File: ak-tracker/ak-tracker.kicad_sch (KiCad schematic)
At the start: 0 parts

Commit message: docs
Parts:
- added U1: (no value), symbol 1_JP:BMA400
- added U2: TPL5010, Package_TO_SOT_SMD:SOT-23-6, symbol Timer:TPL5010
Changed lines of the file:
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@@
 (kicad_sch
-	(version 20250114)
+	(version 20260306)
 	(generator "eeschema")
-	(generator_version "9.0")
+	(generator_version "10.0")
 	(paper "A4")
+	(symbol
+		(lib_id "Timer:TPL5010")
+		(at 73.66 101.6 0)
+		(unit 1)
+		(body_style 1)
+		(exclude_from_sim no)
+		(in_bom yes)
+		(on_board yes)
+		(in_pos_files yes)
+		(dnp no)
+		(fields_autoplaced yes)
+		(property "Reference" "U2"
+			(at 75.8033 88.9 0)
+			(show_name no)
+			(do_not_autoplace no)
+			(effects
+				(font
+					(size 1.27 1.27)
+				)
+				(justify left)
+			)
+		)
+		(property "Value" "TPL5010"
+			(at 75.8033 91.44 0)
+			(show_name no)
+			(do_not_autoplace no)
+			(effects
+				(font
+					(size 1.27 1.27)
+				)
+				(justify left)
+			)
+		)
+		(property "Footprint" "Package_TO_SOT_SMD:SOT-23-6"
+			(at 73.66 101.6 0)
+			(hide yes)
+			(show_name no)
+			(do_not_autoplace no)
+			(effects
+				(font
+					(size 1.27 1.27)
+				)
+			)
+		)
+		(property "Datasheet" "http://www.ti.com/lit/ds/symlink/tpl5010.pdf"
+			(at 68.58 109.22 0)
+			(hide yes)
+			(show_name no)
+			(do_not_autoplace no)
+			(effects
+				(font
+					(size 1.27 1.27)
+				)
+			)
+		)
+		(property "Description" "Timer, Nano Power, Watchdog, 35 nA, 100 ms to 7200 s, VDD 1.8V to 5.5V, Iout max 1mA"
+			(at 73.66 101.6 0)
+			(hide yes)
+			(show_name no)
+			(do_not_autoplace no)
+			(effects
+				(font
+					(size 1.27 1.27)
+				)
+			)
+		)
+		(pin "1"
+		)
+		(pin "2"
+		)
+		(pin "3"
+		)
+		(pin "4"
+		)
+		(pin "5"
+		)
+		(pin "6"
+		)
+		(instances
+			(project "ak-tracker"
+				(path "/c9a4dcbd-d029-4d79-afa4-833091072a3d"
+					(reference "U2")
+					(unit 1)
+				)
+			)
+		)
+	)
+	(symbol
+		(lib_id "1_JP:BMA400")
+		(at 63.5 55.88 0)
+		(unit 1)
+		(body_style 1)
+		(exclude_from_sim no)
+		(in_bom yes)
+		(on_board yes)
+		(in_pos_files yes)
+		(dnp no)
+		(property "Reference" "U1"
+			(at 79.502 49.53 0)
+			(show_name no)
+			(do_not_autoplace no)
+			(effects
+				(font
+					(size 1.27 1.27)
+				)
+			)
+		)
+		(property "Value" ""
+			(at 63.5 55.88 0)
+			(show_name no)
+			(do_not_autoplace no)
+			(effects
+				(font
+					(size 1.27 1.27)
+				)
+			)
+		)
+		(property "Footprint" ""
+			(at 63.5 55.88 0)
+			(hide yes)
+			(show_name no)
+			(do_not_autoplace no)
+			(effects
+				(font
+					(size 1.27 1.27)
+				)
+			)
+		)
+		(property "Datasheet" ""
+			(at 63.5 55.88 0)
+			(hide yes)
+			(show_name no)
+			(do_not_autoplace no)
+			(effects
+				(font
+					(size 1.27 1.27)
+				)
+			)
+		)
+		(property "Description" ""
+			(at 63.5 55.88 0)
+			(hide yes)
+			(show_name no)
+			(do_not_autoplace no)
+			(effects
+				(font
+					(size 1.27 1.27)
+				)
+			)
+		)
+		(pin "8"
+		)
+		(pin "10"
+		)
+		(pin "9"
+		)
+		(pin "6"
+		)
+		(pin "7"
+		)
+		(pin "12"
+		)
+		(pin "4"
+		)
+		(pin "11"
+		)
+		(pin "2"
+		)
+		(pin "3"
+		)
+		(pin "1"
+		)
+		(pin "5"
+		)
+		(instances
+			(project "ak-tracker"
+				(path "/c9a4dcbd-d029-4d79-afa4-833091072a3d"
+					(reference "U1")
+					(unit 1)
+				)
+			)
+		)
+	)
 	(sheet_instances
 		(path "/"

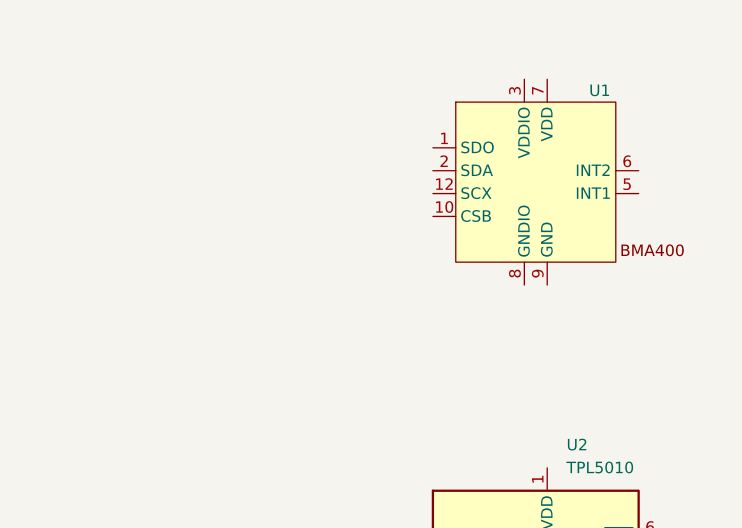
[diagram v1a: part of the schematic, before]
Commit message: TPL5010 and BMA400 as symbols in KiCad
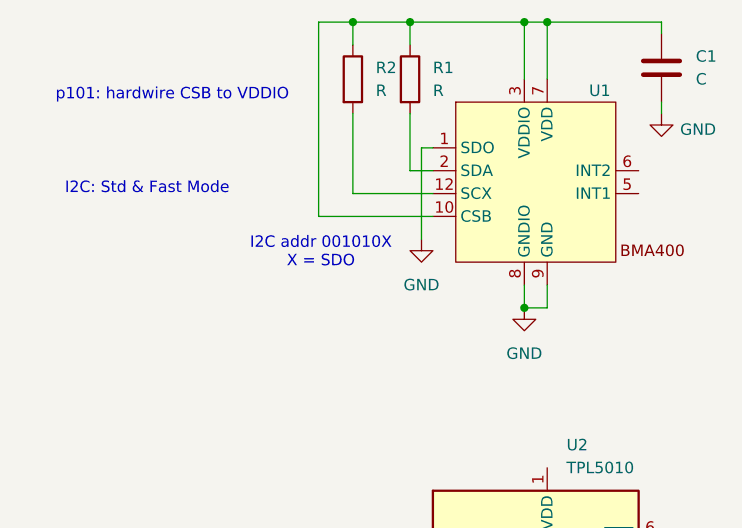
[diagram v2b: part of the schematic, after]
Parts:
- added C1: C, symbol Device:C
- added R1, R2: R, symbol Device:R
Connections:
- net GND: now reaches U1.1 (SDO)
- net GND: now also U1.8 (GNDIO), U1.9 (GND), C1.2
- net at U1.10 (CSB): now also U1.3 (VDDIO), U1.7 (VDD), C1.1, R1.1, R2.1
- net at U1.12 (SCX): now also R2.2
- net at U1.2 (SDA): now also R1.2
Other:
- note added: "I2C addr 001010X X = SDO"
- note added: "I2C: Std & Fast Mode"
- note added: "p101: hardwire CSB to VDDIO"

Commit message: initial schematic
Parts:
- added C2: C, symbol Device:C
- added J1: left, Connector_PinHeader_2.54mm:PinHeader_1x18_P2.54mm_Vertical, symbol Connector_Generic:Conn_01x18
- added J2: right, Connector_PinHeader_2.54mm:PinHeader_1x18_P2.54mm_Vertical, symbol Connector_Generic:Conn_01x18
- added R3, R4: 47k, symbol Device:R
- added SW1: Reset, symbol Switch:SW_Push
- added SW2: SW_DIP_x01, symbol Switch:SW_DIP_x01
- U1: value (none) -> BMA400
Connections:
- net GND: now also U2.2 (GND), C2.2, J1.2 (Pin_2), J2.2 (Pin_2), R4.2
- net at U2.1 (VDD): now also C2.1, R3.1, SW1.2, SW2.1
- net at U2.3 (DELAY/M_RST): now also R4.1, SW1.1
- net WOKE: now reaches U2.4 (DONE)
- net WAKE: now reaches U2.5 (WAKE)
- net ~{RST}: now reaches U2.6 (~{RST})
- net ~{RST}: now also J2.18 (Pin_18), R3.2
- net VCC: now reaches C1.1, R1.1, R2.1, U1.10 (CSB), U1.3 (VDDIO), U1.7 (VDD)
- net VCC: now also J2.3 (Pin_3), SW2.2
- net SCL: now reaches R2.2, U1.12 (SCX)
- net SCL: now also J1.6 (Pin_6)
- net SDA: now reaches R1.2, U1.2 (SDA)
- net SDA: now also J1.7 (Pin_7)
- new net VEXT: J1.3 (Pin_3)
- no-connect marks 0 -> 4
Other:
- note added: "2 x 18 x 2.54 mm 25.4? mm apart"
- note added: "~6min"
- moved on the sheet: R1, R2

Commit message: footprints
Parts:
- removed SW2: SW_DIP_x01, symbol Switch:SW_DIP_x01
- added SW3: SW_DIP_x02, Button_Switch_SMD:SW_DIP_SPSTx02_Slide_6.7x6.64mm_W6.73mm_P2.54mm_LowProfile_JPin, symbol Switch:SW_DIP_x02
- C1, C2: footprint (none) -> Capacitor_SMD:C_0805_2012Metric_Pad1.18x1.45mm_HandSolder
- R1, R2: value R -> 2k2; footprint (none) -> Resistor_SMD:R_0805_2012Metric_Pad1.20x1.40mm_HandSolder
- R3: value 47k -> 100k; footprint (none) -> Resistor_SMD:R_0805_2012Metric_Pad1.20x1.40mm_HandSolder
- R4: footprint (none) -> Resistor_SMD:R_0805_2012Metric_Pad1.20x1.40mm_HandSolder
- SW1: footprint (none) -> Button_Switch_SMD:SW_Push_1P1T_NO_CK_KSC9xxG
- U1: footprint (none) -> Package_LGA:LGA-12_2x2mm_P0.5mm
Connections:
- net VCC: now also SW3.3, SW3.4; no longer C1.1, R1.1, R2.1, U1.10 (CSB), U1.3 (VDDIO), U1.7 (VDD)
- net WAKE: now also J2.8 (Pin_8)
- net WOKE: now also J2.7 (Pin_7)
- net at C2.1, R3.1, SW1.2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: now also SW3.2
- net MOVED: now reaches J2.6 (Pin_6)
- net MOVED: now also U1.5 (INT1)
- new net: C1.1, R1.1, R2.1, SW3.1, U1.10 (CSB), U1.3 (VDDIO), U1.7 (VDD)
- no-connect marks 4 -> 27
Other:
- note added: "For BMI270, use BMI160 symbol"
- note added: "No intr really needed for atonomous mode"

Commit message: initial routing
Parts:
- removed SW1: Reset, Button_Switch_SMD:SW_Push_1P1T_NO_CK_KSC9xxG, symbol Switch:SW_Push
- added R5: 0, Resistor_SMD:R_0805_2012Metric_Pad1.20x1.40mm_HandSolder, symbol Device:R
- added SW2: Reset, Button_Switch_SMD:SW_Push_1P1T_NO_CK_KSC9xxG, symbol Switch:SW_Push
- SW3: footprint Button_Switch_SMD:SW_DIP_SPSTx02_Slide_6.7x6.64mm_W6.73mm_P2.54mm_LowProfile_JPin -> Button_Switch_SMD:SW_DIP_SPSTx02_Slide_9.78x7.26mm_W8.61mm_P2.54mm
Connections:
- net VDD2: now reaches C2.1, R3.1, U2.1 (VDD)
- net VDD2: now also SW3.1, SW2.2; no longer SW3.2
- net at R4.1, U2.3 (DELAY/M_RST): now also SW2.1
- net VDD1: now reaches C1.1, R2.1, U1.10 (CSB), U1.7 (VDD)
- net VDD1: now also SW3.2, R5.2; no longer R1.1, SW3.1, U1.3 (VDDIO)
- new net: R1.1, R5.1, U1.3 (VDDIO)

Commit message: better routing
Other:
- moved on the sheet: R1, R2, R5

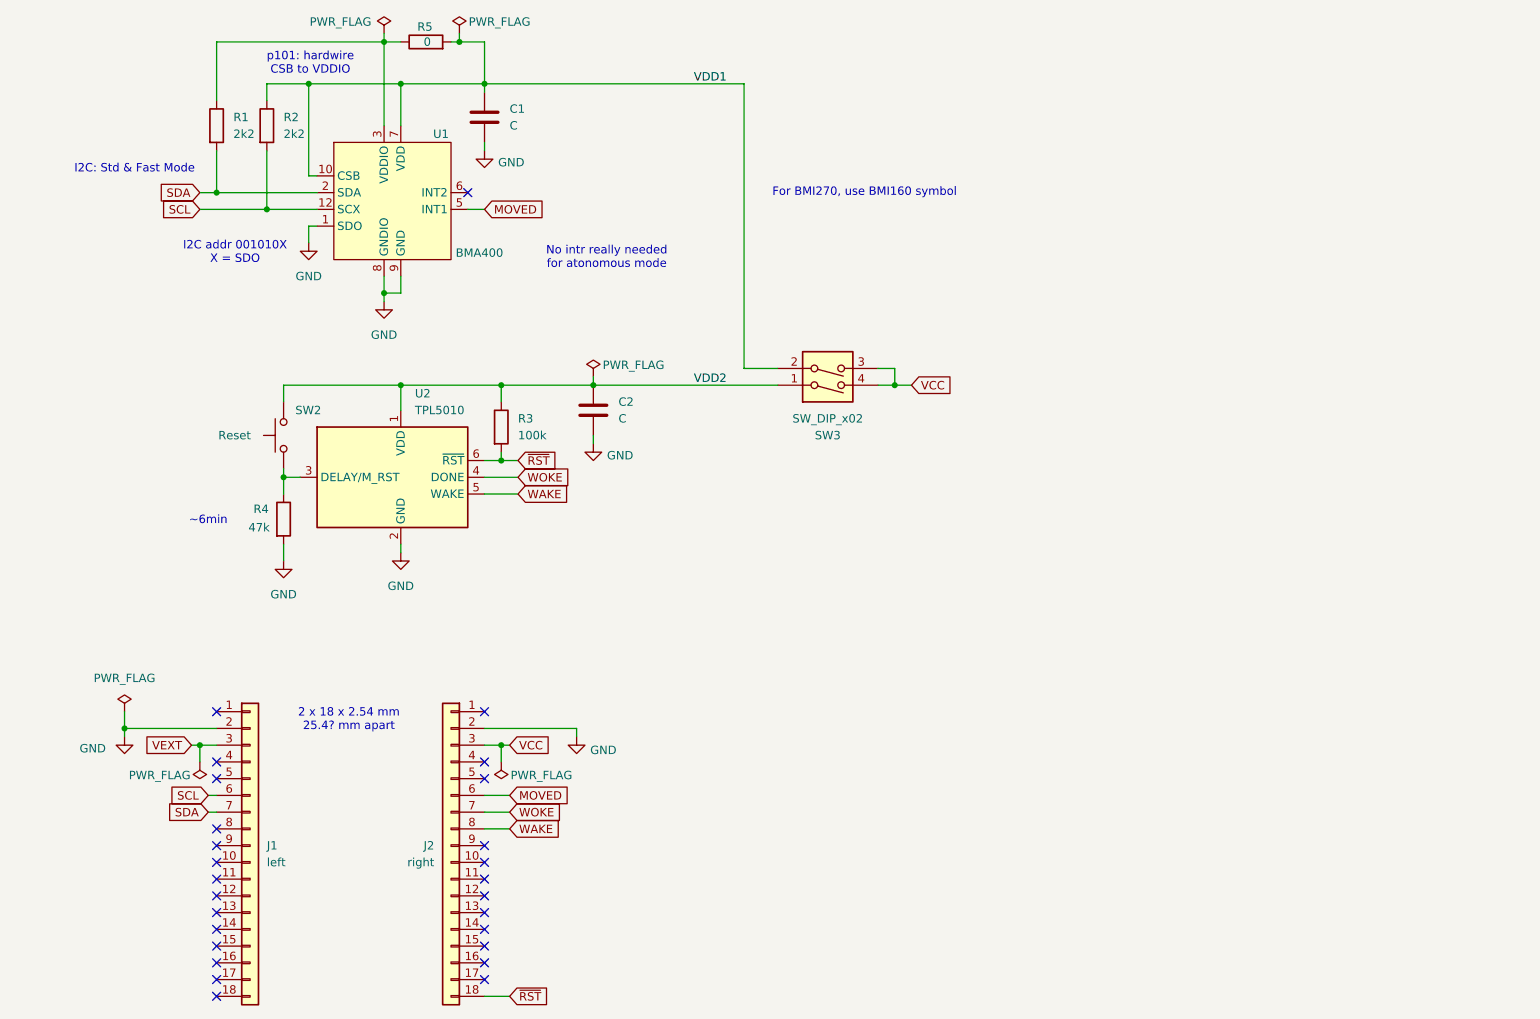
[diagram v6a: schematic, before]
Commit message: interrupts to 5,6,7
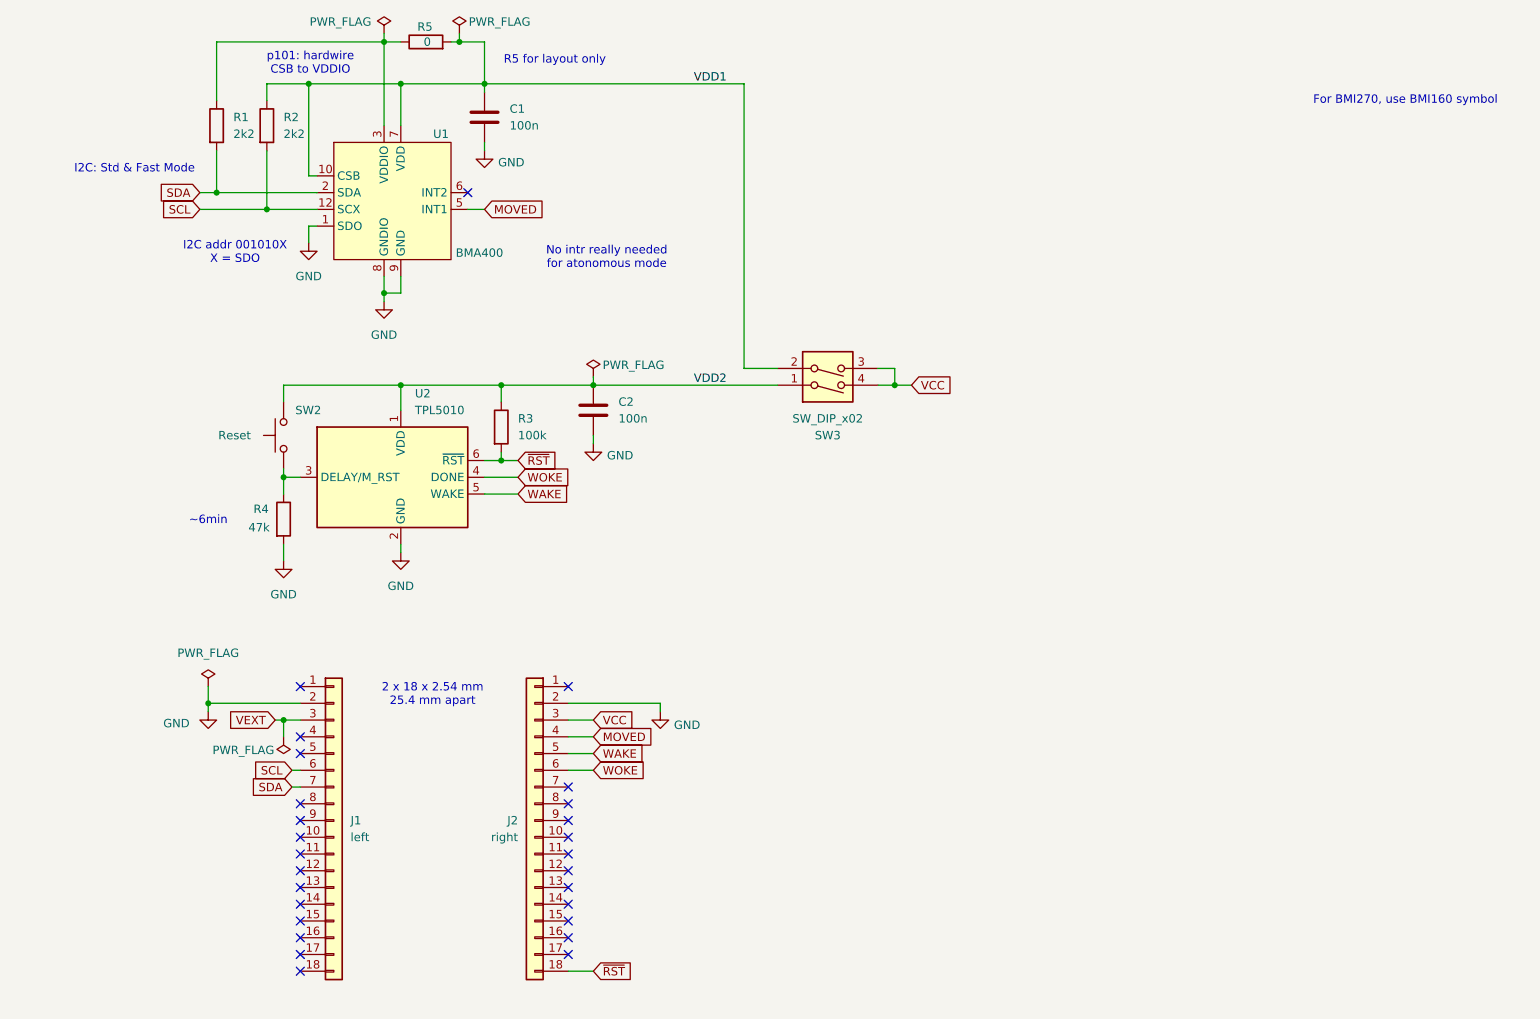
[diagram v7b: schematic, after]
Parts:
- C1, C2: value C -> 100n
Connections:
- net MOVED: now also J2.4 (Pin_4); no longer J2.6 (Pin_6)
- net WAKE: now also J2.5 (Pin_5); no longer J2.8 (Pin_8)
- net WOKE: now also J2.6 (Pin_6); no longer J2.7 (Pin_7)
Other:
- note added: "2 x 18 x 2.54 mm 25.4 mm apart"
- note added: "R5 for layout only"
- note removed: "2 x 18 x 2.54 mm 25.4? mm apart"
- moved on the sheet: J1, J2

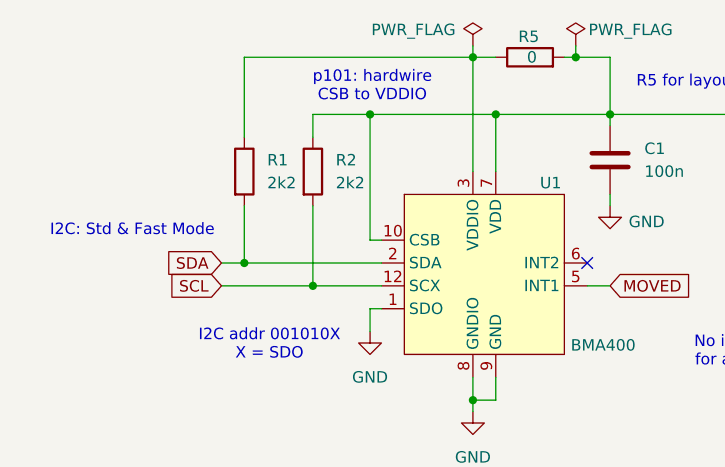
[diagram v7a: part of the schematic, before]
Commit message: smaller i2c pullup
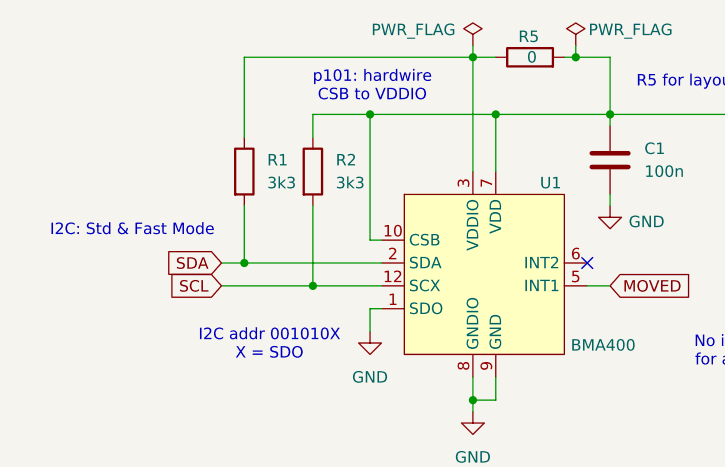
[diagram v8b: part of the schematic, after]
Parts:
- R1, R2: value 2k2 -> 3k3
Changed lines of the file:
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@@
 			)
 		)
-		(property "Value" "2k2"
+		(property "Value" "3k3"
 			(at 48.26 49.5299 0)
 			(show_name no)
@@
 			)
 		)
-		(property "Value" "2k2"
+		(property "Value" "3k3"
 			(at 55.88 49.5299 0)
 			(show_name no)
